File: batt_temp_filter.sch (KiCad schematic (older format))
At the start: 4 parts

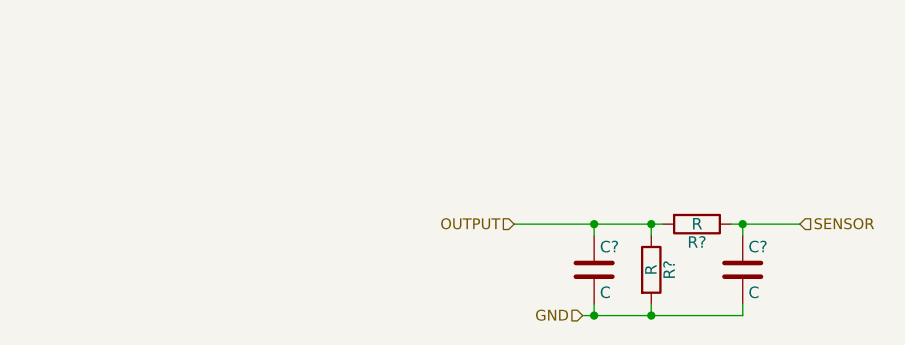
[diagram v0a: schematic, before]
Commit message: added some ICs, started on power, changed sheet sizes
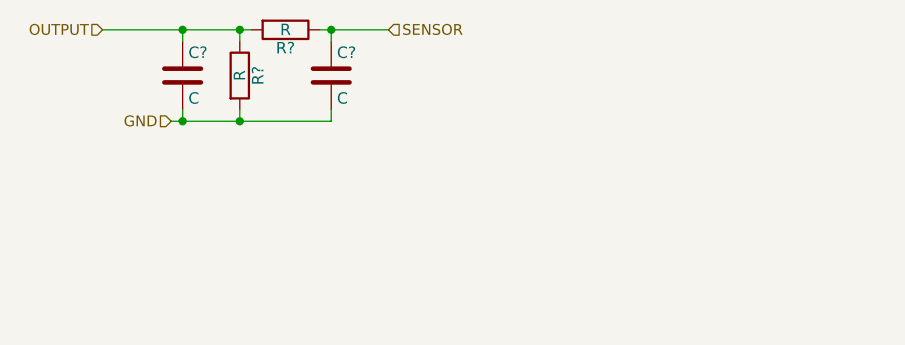
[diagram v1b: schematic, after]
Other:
- moved on the sheet: C?, R?
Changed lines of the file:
@@
 EELAYER 25 0
 EELAYER END
-$Descr A4 11693 8268
+$Descr User 7874 5906
 encoding utf-8
 Sheet 6 12
@@
 L R R?
 U 1 1 572948B6
-P 5850 3350
-F 0 "R?" V 5930 3350 50  0000 C CNN
-F 1 "R" V 5850 3350 50  0000 C CNN
-F 2 "" V 5780 3350 50  0000 C CNN
-F 3 "" H 5850 3350 50  0000 C CNN
-	1    5850 3350
+P 4050 2500
+F 0 "R?" V 4130 2500 50  0000 C CNN
+F 1 "R" V 4050 2500 50  0000 C CNN
+F 2 "" V 3980 2500 50  0000 C CNN
+F 3 "" H 4050 2500 50  0000 C CNN
+	1    4050 2500
 	0    1    1    0
 $EndComp
@@
 L R R?
 U 1 1 57294A75
-P 5650 3550
-F 0 "R?" V 5730 3550 50  0000 C CNN
-F 1 "R" V 5650 3550 50  0000 C CNN
-F 2 "" V 5580 3550 50  0000 C CNN
-F 3 "" H 5650 3550 50  0000 C CNN
-	1    5650 3550
+P 3850 2700
+F 0 "R?" V 3930 2700 50  0000 C CNN
+F 1 "R" V 3850 2700 50  0000 C CNN
+F 2 "" V 3780 2700 50  0000 C CNN
+F 3 "" H 3850 2700 50  0000 C CNN
+	1    3850 2700
 	1    0    0    -1
 $EndComp
@@
 L C C?
 U 1 1 57294ABC
-P 5400 3550
-F 0 "C?" H 5425 3650 50  0000 L CNN
-F 1 "C" H 5425 3450 50  0000 L CNN
-F 2 "" H 5438 3400 50  0000 C CNN
-F 3 "" H 5400 3550 50  0000 C CNN
-	1    5400 3550
+P 3600 2700
+F 0 "C?" H 3625 2800 50  0000 L CNN
+F 1 "C" H 3625 2600 50  0000 L CNN
+F 2 "" H 3638 2550 50  0000 C CNN
+F 3 "" H 3600 2700 50  0000 C CNN
+	1    3600 2700
 	1    0    0    -1
 $EndComp
@@
 L C C?
 U 1 1 57294B05
-P 6050 3550
-F 0 "C?" H 6075 3650 50  0000 L CNN
-F 1 "C" H 6075 3450 50  0000 L CNN
-F 2 "" H 6088 3400 50  0000 C CNN
-F 3 "" H 6050 3550 50  0000 C CNN
-	1    6050 3550
+P 4250 2700
+F 0 "C?" H 4275 2800 50  0000 L CNN
+F 1 "C" H 4275 2600 50  0000 L CNN
+F 2 "" H 4288 2550 50  0000 C CNN
+F 3 "" H 4250 2700 50  0000 C CNN
+	1    4250 2700
 	1    0    0    -1
 $EndComp
 Wire Wire Line
-	6000 3350 6300 3350
+	4200 2500 4500 2500
 Wire Wire Line
-	6050 3350 6050 3400
-Connection ~ 6050 3350
-Text HLabel 6300 3350 2    47   Input ~ 0
+	4250 2500 4250 2550
+Connection ~ 4250 2500
+Text HLabel 4500 2500 2    47   Input ~ 0
 SENSOR
 Wire Wire Line
-	5700 3350 5050 3350
-Text HLabel 5050 3350 0    47   Input ~ 0
+	3900 2500 3250 2500
+Text HLabel 3250 2500 0    47   Input ~ 0
 OUTPUT
 Wire Wire Line
-	5400 3400 5400 3350
-Connection ~ 5400 3350
+	3600 2550 3600 2500
+Connection ~ 3600 2500
 Wire Wire Line
-	5650 3400 5650 3350
-Connection ~ 5650 3350
+	3850 2550 3850 2500
+Connection ~ 3850 2500
 Wire Wire Line
-	5400 3700 5400 3750
+	3600 2850 3600 2900
 Wire Wire Line
-	5350 3750 6050 3750
+	3550 2900 4250 2900
 Wire Wire Line
-	6050 3750 6050 3700
+	4250 2900 4250 2850
 Wire Wire Line
-	5650 3700 5650 3750
-Connection ~ 5650 3750
-Connection ~ 5400 3750
-Text HLabel 5350 3750 0    47   Input ~ 0
+	3850 2850 3850 2900
+Connection ~ 3850 2900
+Connection ~ 3600 2900
+Text HLabel 3550 2900 0    47   Input ~ 0
 GND
 $EndSCHEMATC
